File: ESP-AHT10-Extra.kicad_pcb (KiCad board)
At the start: 2 copper layers, 38.2 x 20.8 mm, 26 parts, among them J1 USB, SW1 RESET, SW2 PROG, U1 CH330N, U2 HT7233, U3 ESP-12, U4 AHT10, U5 USBLC6-2SC6

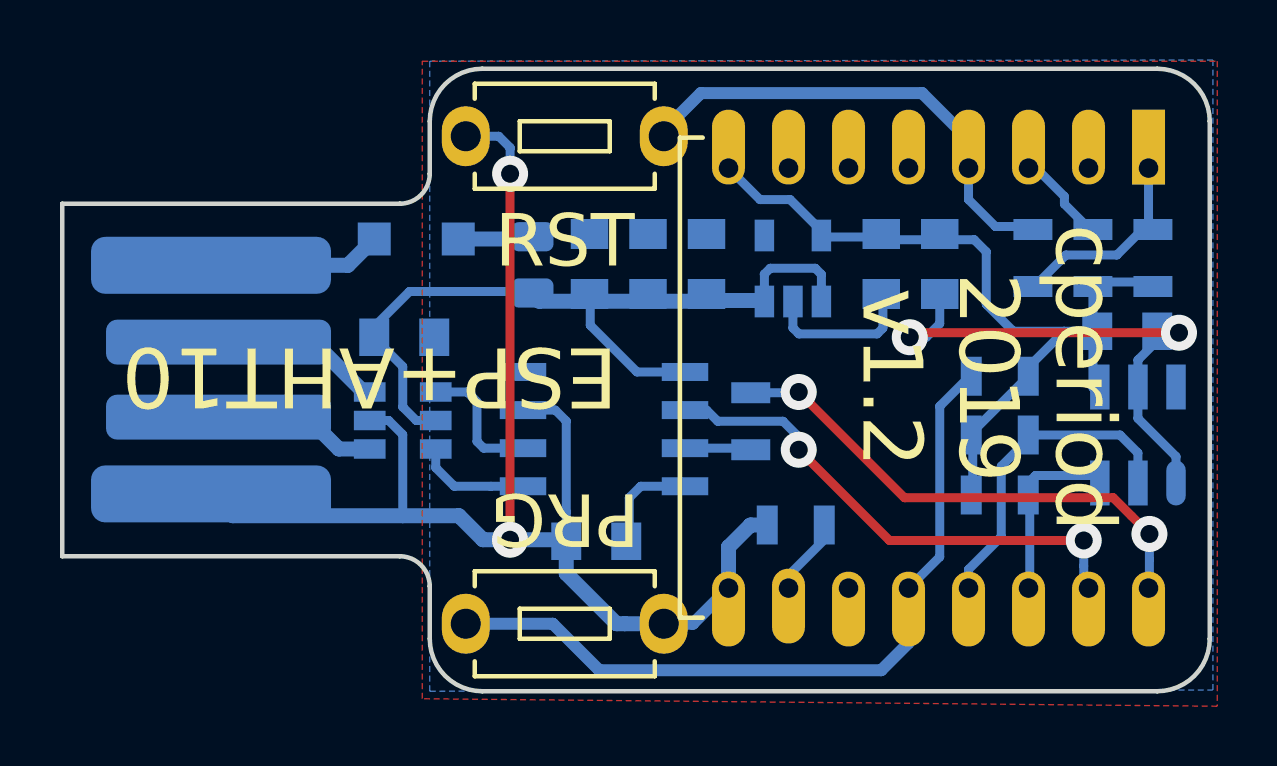
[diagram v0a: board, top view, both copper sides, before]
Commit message: really no excuse not to connect RTS to RESET
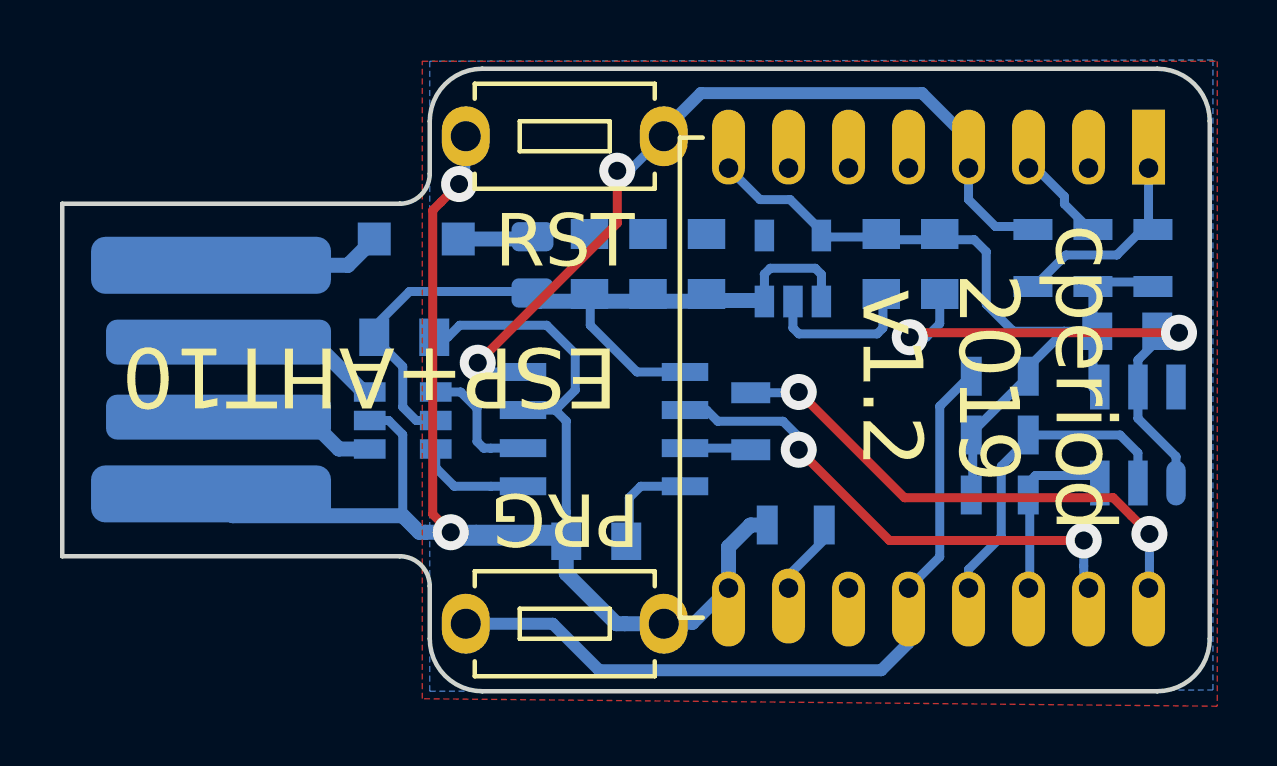
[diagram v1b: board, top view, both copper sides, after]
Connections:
- R2 pad 2: Net-(R2-Pad2) -> RESET
- SW1 pad 1: Net-(R2-Pad2) -> RESET
- U1 pad 4: (no net) -> RESET
- U3 pad 4: Net-(R2-Pad2) -> RESET
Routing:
- net RESET: track 0.00 -> 28.0 mm, vias 0 -> 2
- net Net-(R2-Pad2): track 16.0 -> 0.00 mm
- net GND: track 71.1 -> 79.8 mm

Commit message: fix R8's value
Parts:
- R8: value 330R -> 470R
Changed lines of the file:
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@@
       (effects (font (size 1 1) (thickness 0.15)) (justify mirror))
     )
-    (fp_text value 330R (at -0.1 -10.85 270) (layer B.Fab)
+    (fp_text value 470R (at -14.2 0 270) (layer B.Fab)
       (effects (font (size 1 1) (thickness 0.15)) (justify mirror))
     )

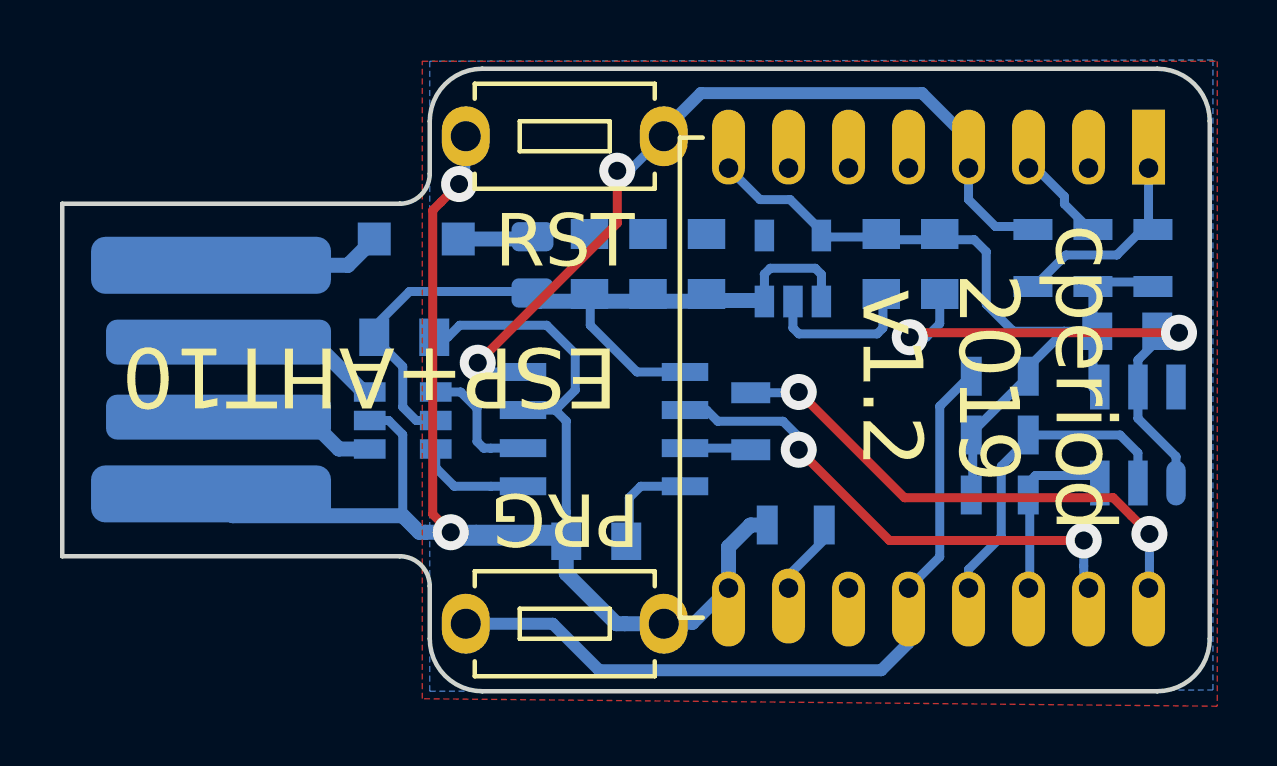
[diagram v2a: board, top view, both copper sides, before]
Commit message: leave a bit more meat on the ground pours
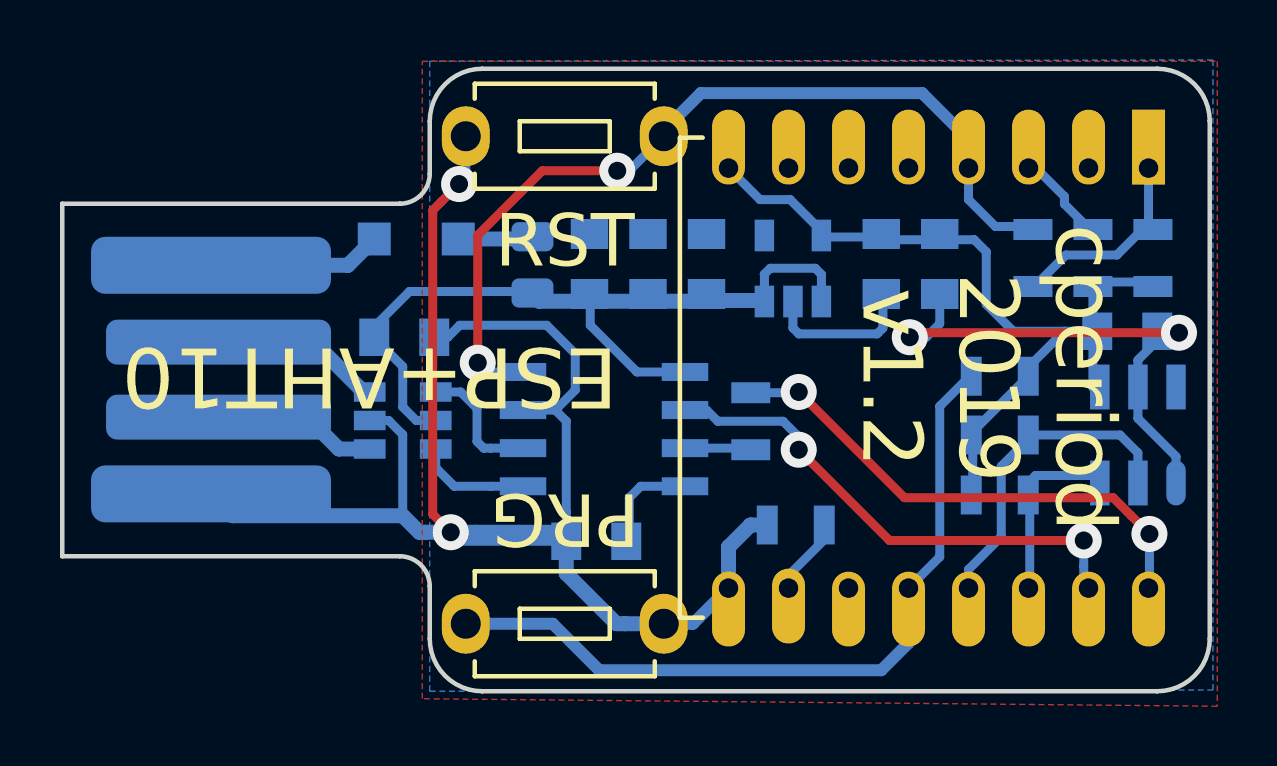
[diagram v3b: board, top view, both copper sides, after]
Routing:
- net RESET: track 28.0 -> 29.5 mm
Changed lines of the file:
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@@
     (thickness 1.6)
     (drawings 18)
-    (tracks 210)
+    (tracks 211)
     (zones 0)
     (modules 26)
@@
   (segment (start 144.157374 97.107374) (end 143.85 96.8) (width 0.3) (layer B.Cu) (net 20))
   (via (at 148.5 90.4) (size 1.2) (drill 0.6) (layers F.Cu B.Cu) (net 20))
-  (segment (start 143.85 96.8) (end 148.5 92.15) (width 0.3) (layer F.Cu) (net 20))
-  (segment (start 148.5 92.15) (end 148.5 90.4) (width 0.3) (layer F.Cu) (net 20))
   (segment (start 148.9 90.4) (end 150.05 89.25) (width 0.3) (layer B.Cu) (net 20))
   (segment (start 148.5 90.4) (end 148.9 90.4) (width 0.3) (layer B.Cu) (net 20))
+  (segment (start 146 90.4) (end 148.5 90.4) (width 0.3) (layer F.Cu) (net 20))
+  (segment (start 143.85 96.8) (end 143.85 92.55) (width 0.3) (layer F.Cu) (net 20))
+  (segment (start 143.85 92.55) (end 146 90.4) (width 0.3) (layer F.Cu) (net 20))
   (zone (net 0) (net_name "") (layers F&B.Cu) (hatch edge 0.508)
     (connect_pads (clearance 0.508))

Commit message: try adding a WLED.
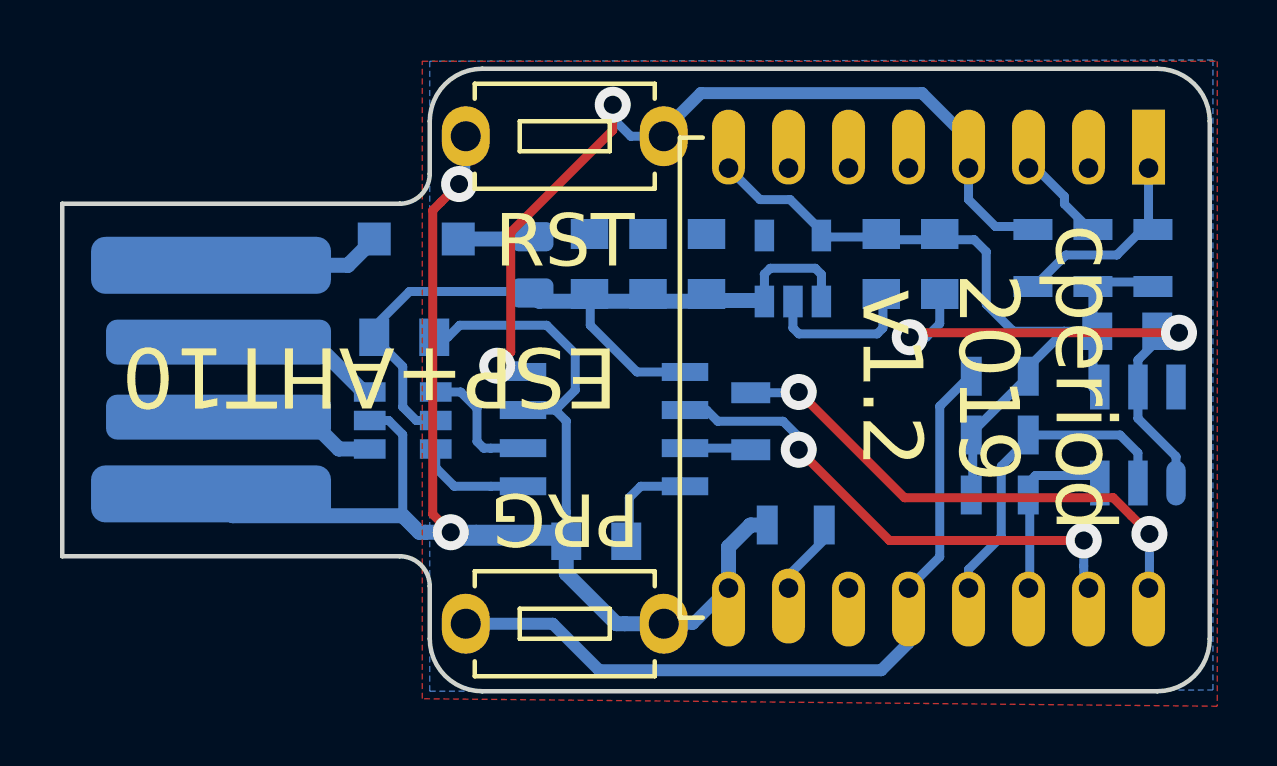
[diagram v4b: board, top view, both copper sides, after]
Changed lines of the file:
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@@
     (thickness 1.6)
     (drawings 18)
-    (tracks 211)
+    (tracks 214)
     (zones 0)
     (modules 26)
@@
   (segment (start 145.525 92.675) (end 145.675 92.825) (width 0.5) (layer B.Cu) (net 19))
   (segment (start 143.2 92.675) (end 145.525 92.675) (width 0.5) (layer B.Cu) (net 19))
-  (segment (start 145.359217 97.107374) (end 144.157374 97.107374) (width 0.3) (layer B.Cu) (net 20))
-  (via (at 143.85 96.8) (size 1.2) (drill 0.6) (layers F.Cu B.Cu) (net 20))
-  (segment (start 144.157374 97.107374) (end 143.85 96.8) (width 0.3) (layer B.Cu) (net 20))
-  (via (at 148.5 90.4) (size 1.2) (drill 0.6) (layers F.Cu B.Cu) (net 20))
-  (segment (start 148.9 90.4) (end 150.05 89.25) (width 0.3) (layer B.Cu) (net 20))
-  (segment (start 148.5 90.4) (end 148.9 90.4) (width 0.3) (layer B.Cu) (net 20))
-  (segment (start 146 90.4) (end 148.5 90.4) (width 0.3) (layer F.Cu) (net 20))
-  (segment (start 143.85 96.8) (end 143.85 92.55) (width 0.3) (layer F.Cu) (net 20))
-  (segment (start 143.85 92.55) (end 146 90.4) (width 0.3) (layer F.Cu) (net 20))
+  (via (at 144.5 96.9) (size 1.2) (drill 0.6) (layers F.Cu B.Cu) (net 20))
+  (segment (start 145.348528 96.9) (end 144.5 96.9) (width 0.3) (layer B.Cu) (net 20))
+  (segment (start 145.359217 96.910689) (end 145.348528 96.9) (width 0.3) (layer B.Cu) (net 20))
+  (segment (start 145.359217 97.107374) (end 145.359217 96.910689) (width 0.3) (layer B.Cu) (net 20))
+  (segment (start 148.35 88.65) (end 148.35 88.2) (width 0.3) (layer B.Cu) (net 20))
+  (segment (start 148.95 89.25) (end 148.35 88.65) (width 0.3) (layer B.Cu) (net 20))
+  (via (at 148.35 88.2) (size 1.2) (drill 0.6) (layers F.Cu B.Cu) (net 20))
+  (segment (start 150.05 89.25) (end 148.95 89.25) (width 0.3) (layer B.Cu) (net 20))
+  (segment (start 148.35 89.048528) (end 148.35 88.2) (width 0.3) (layer F.Cu) (net 20))
+  (segment (start 144.95 92.448528) (end 148.35 89.048528) (width 0.3) (layer F.Cu) (net 20))
+  (segment (start 144.5 96.9) (end 144.95 96.45) (width 0.3) (layer F.Cu) (net 20))
+  (segment (start 144.95 96.45) (end 144.95 92.448528) (width 0.3) (layer F.Cu) (net 20))
   (zone (net 0) (net_name "") (layers F&B.Cu) (hatch edge 0.508)
     (connect_pads (clearance 0.508))

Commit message: place WLED, tidy up after some footprint changes
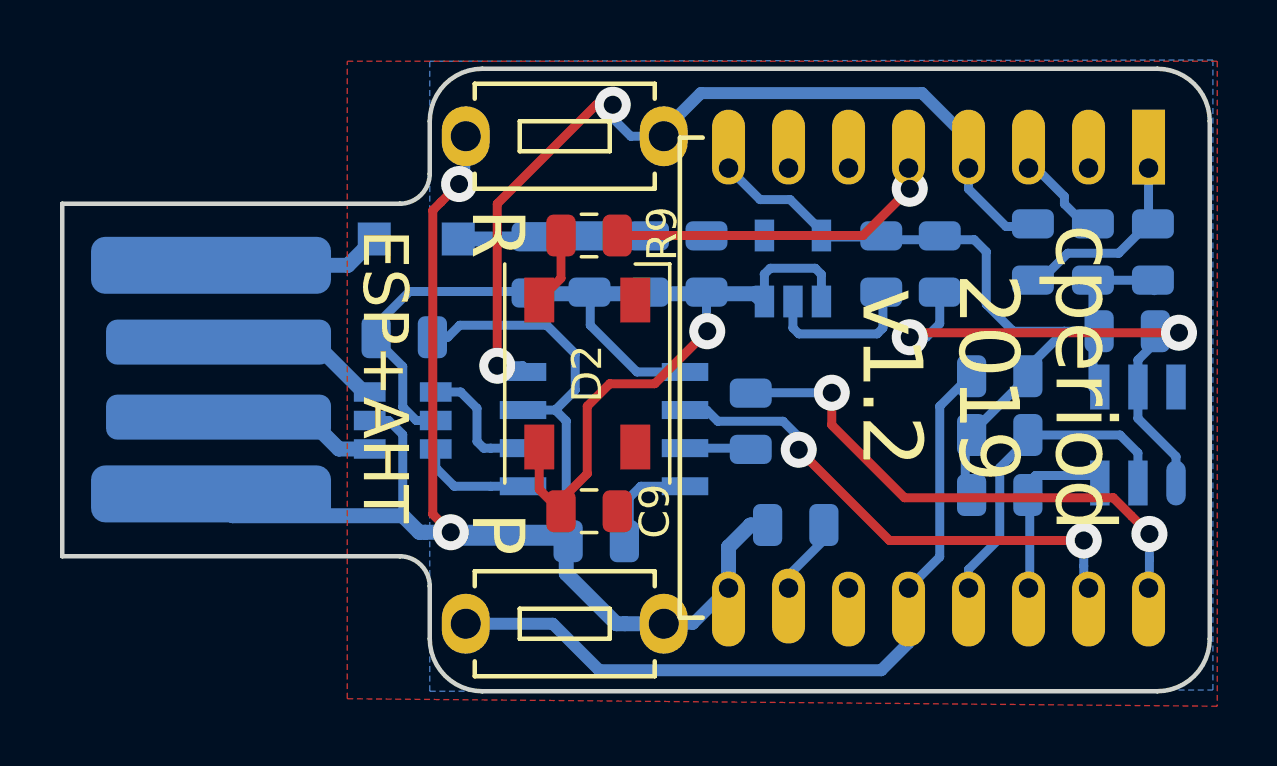
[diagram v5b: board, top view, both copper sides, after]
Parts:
- added C9: 47u, Capacitor_SMD:C_0805_2012Metric, F.Cu at (147.6, 101.8)
- added D2: SK6812, LED_SMD:LED_SK6812_PLCC4_5.0x5.0mm_P3.2mm, F.Cu at (147.5, 97.2)
- added R9: 470R, Resistor_SMD:R_0805_2012Metric, F.Cu at (147.6, 92.6)
- C1, C2, C3, C4, C5, C6, C7, C8: footprint Capacitors_SMD:C_0805 -> Capacitor_SMD:C_0805_2012Metric
- D1: footprint Diodes_SMD:D_SOD-123F -> Diode_SMD:D_SOD-123F
- R1, R2, R3, R4, R5, R6, R7, R8: footprint Resistors_SMD:R_0805 -> Resistor_SMD:R_0805_2012Metric
- moved R1 0.20 mm to (164.4, 93.1)
- moved R2 0.20 mm to (162.4, 93.1)
- moved R3 0.20 mm to (166.4, 93.1)
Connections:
- U3 pad 5: (no net) -> WLED
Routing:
- net 5V: track 27.0 -> 39.7 mm, vias 0 -> 1
- net WLED: track 0.00 -> 11.1 mm, vias 0 -> 1
- net Net-(D2-Pad2): track 0.00 -> 2.45 mm
- net eTX: track 17.1 -> 17.7 mm
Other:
- board text added: "ESP+AHT"
- board text added: "P"
- board text added: "R"
- board text removed: "ESP+AHT10"
- board text removed: "PRG"
- board text removed: "RST"

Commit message: more tweaking
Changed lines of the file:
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@@
     (thickness 1.6)
     (drawings 19)
-    (tracks 233)
+    (tracks 235)
     (zones 0)
     (modules 29)
@@
   )
   (layers
-    (0 F.Cu signal hide)
-    (31 B.Cu signal)
+    (0 F.Cu signal)
+    (31 B.Cu signal hide)
     (32 B.Adhes user hide)
     (33 F.Adhes user hide)
-    (34 B.Paste user)
-    (35 F.Paste user hide)
-    (36 B.SilkS user)
-    (37 F.SilkS user hide)
-    (38 B.Mask user)
-    (39 F.Mask user hide)
+    (34 B.Paste user hide)
+    (35 F.Paste user)
+    (36 B.SilkS user hide)
+    (37 F.SilkS user)
+    (38 B.Mask user hide)
+    (39 F.Mask user)
     (40 Dwgs.User user hide)
     (41 Cmts.User user hide)
@@
     (44 Edge.Cuts user)
     (45 Margin user hide)
-    (46 B.CrtYd user)
-    (47 F.CrtYd user hide)
-    (48 B.Fab user)
-    (49 F.Fab user hide)
+    (46 B.CrtYd user hide)
+    (47 F.CrtYd user)
+    (48 B.Fab user hide)
+    (49 F.Fab user)
   )
   (setup
@@
   (segment (start 162.355703 92.25862) (end 161.45862 92.25862) (width 0.3) (layer B.Cu) (net 20))
   (segment (start 161.45862 92.25862) (end 160.209217 91.009217) (width 0.3) (layer B.Cu) (net 20))
-  (segment (start 146.625 93.985001) (end 145.9 94.710001) (width 0.3) (layer F.Cu) (net 21))
-  (segment (start 146.625 92.55862) (end 146.625 93.985001) (width 0.3) (layer F.Cu) (net 21))
+  (segment (start 145.95 94.660001) (end 145.9 94.710001) (width 0.3) (layer F.Cu) (net 21))
+  (segment (start 145.95 93.45) (end 145.95 94.660001) (width 0.3) (layer F.Cu) (net 21))
+  (segment (start 146.625 92.55862) (end 146.625 92.775) (width 0.3) (layer F.Cu) (net 21))
+  (segment (start 146.625 92.775) (end 145.95 93.45) (width 0.3) (layer F.Cu) (net 21))
   (segment (start 158.209217 90.312374) (end 158.187626 90.312374) (width 0.3) (layer F.Cu) (net 22))
   (via (at 158.25 91) (size 1.2) (drill 0.6) (layers F.Cu B.Cu) (net 22))
